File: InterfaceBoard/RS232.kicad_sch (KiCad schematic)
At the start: 0 parts

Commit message: InterfaceBoard: Add RS-232/DE-9
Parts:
- added C23, C24, C25, C26, C27: 1uF, Capacitor_SMD:C_0603_1608Metric, symbol Device:C_Small
- added J4: DB9_Female_MountingHoles, lib:ASSMANN_A-DF_09_A_KG-T2S, symbol Connector:DB9_Female_MountingHoles
- added R77: 0, Resistor_SMD:R_0603_1608Metric, symbol Device:R_Small
- added U3: MAX232, Package_SO:SOIC-16_3.9x9.9mm_P1.27mm, symbol Interface_UART:MAX232
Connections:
- new net: C24.1, U3.4 (C2+)
- new net: C24.2, U3.5 (C2-)
- new net: J4.0 (PAD), R77.1
- new net: C23.1, U3.1 (C1+)
- new net: C23.2, U3.3 (C1-)
- new net: J4.3, U3.13 (R1IN)
- new net: J4.2, U3.14 (T1OUT)
- new net: C25.1, U3.2 (VS+)
- new net: C26.1, U3.6 (VS-)
- new net: J4.8, U3.7 (T2OUT)
- new net: J4.7, U3.8 (R2IN)
- new net +5V: C27.1, U3.16 (VCC)
- new net GND: C25.2, C26.2, C27.2, J4.5, R77.2, U3.15 (GND)
- new net RS232_CTS: U3.10 (T2IN)
- new net RS232_RTS: U3.9 (R2OUT)
- new net RS232_RX: U3.12 (R1OUT)
- new net RS232_TX: U3.11 (T1IN)

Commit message: InterfaceBoard: Add 3.3 V regulater, test points.
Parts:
- U3: DigiKey (none) -> https://www.digikey.com/en/products/detail/texas-instrument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
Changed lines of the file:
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@@
+      (effects (font (size 1.27 1.27)) hide)
+    )
+    (property "DigiKey" "https://www.digikey.com/en/products/detail/texas-instruments/MAX232IDR/1511034" (id 4) (at 207.01 91.44 0)
       (effects (font (size 1.27 1.27)) hide)
     )

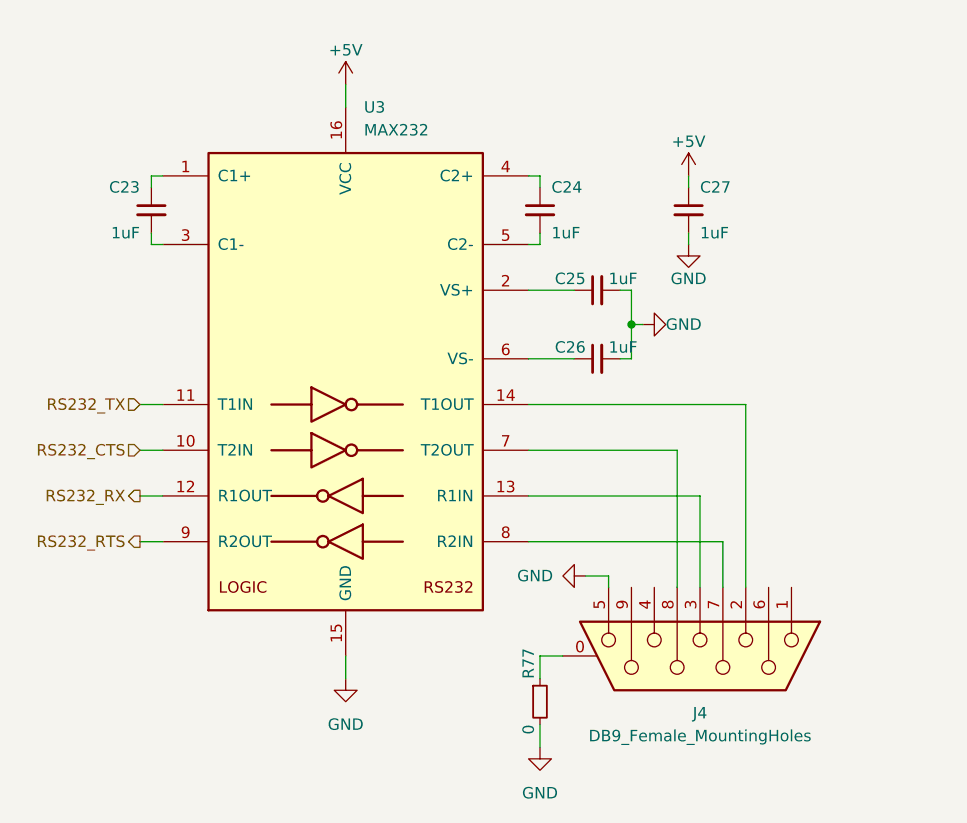
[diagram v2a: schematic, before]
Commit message: InterfaceBoard: MAX232 -> MAX3232
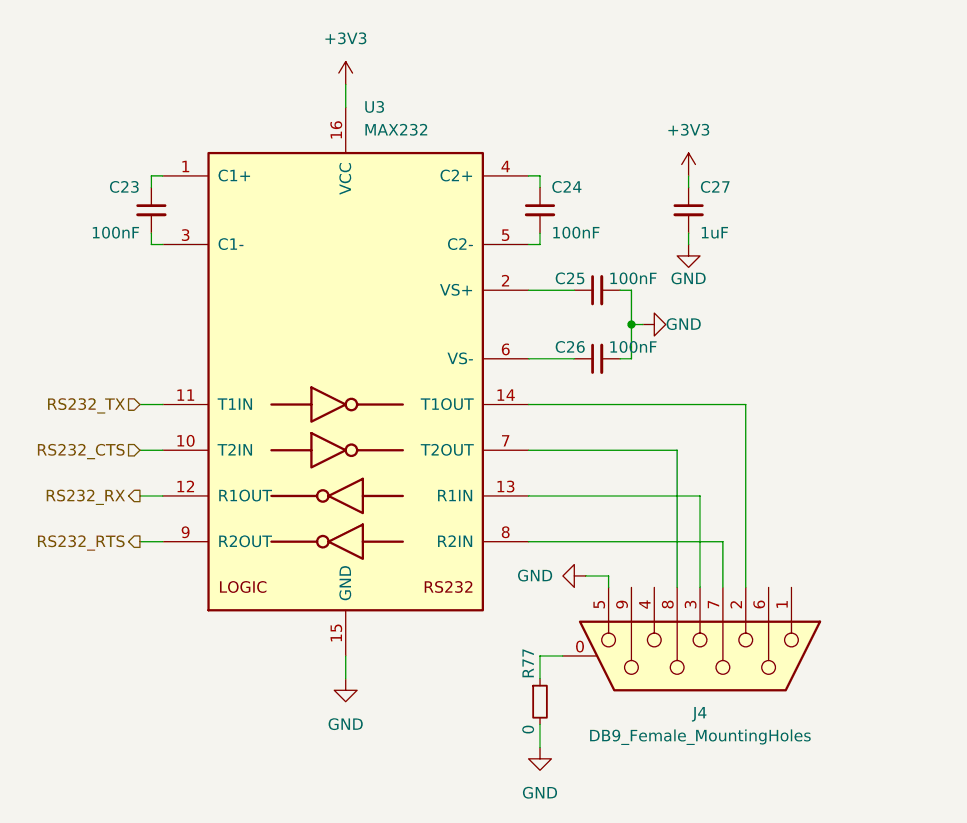
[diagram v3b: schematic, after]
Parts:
- C23, C24, C25, C26: value 1uF -> 100nF
- U3: symbol Interface_UART:MAX232 -> Interface_UART:MAX3232
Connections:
- net +5V renamed +3V3
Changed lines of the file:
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@@
     (effects (font (size 1.27 1.27)) (justify right))
   )
+  (symbol (lib_id "power:+3V3") (at 207.01 58.42 0) (unit 1)
+    (in_bom yes) (on_board yes) (fields_autoplaced)
+    (property "Reference" "#PWR?" (id 0) (at 207.01 62.23 0)
+      (effects (font (size 1.27 1.27)) hide)
+    )
+    (property "Value" "+3V3" (id 1) (at 207.01 53.34 0))
+    (property "Footprint" "" (id 2) (at 207.01 58.42 0)
+      (effects (font (size 1.27 1.27)) hide)
+    )
+    (property "Datasheet" "" (id 3) (at 207.01 58.42 0)
+      (effects (font (size 1.27 1.27)) hide)
+    )
+    (pin "1")
+  )
   (symbol (lib_id "Device:C_Small") (at 228.6 72.39 0) (mirror y) (unit 1)
     (in_bom yes) (on_board yes)
@@
       (effects (font (size 1.27 1.27)) (justify right))
     )
-    (property "Value" "1uF" (id 1) (at 229.87 74.93 0)
+    (property "Value" "100nF" (id 1) (at 229.87 74.93 0)
       (effects (font (size 1.27 1.27)) (justify right))
     )
@@
     (pin "2")
   )
-  (symbol (lib_id "power:+5V") (at 207.01 58.42 0) (unit 1)
-    (in_bom yes) (on_board yes)
-    (property "Reference" "#PWR0153" (id 0) (at 207.01 62.23 0)
-      (effects (font (size 1.27 1.27)) hide)
-    )
-    (property "Value" "+5V" (id 1) (at 207.01 54.61 0))
-    (property "Footprint" "" (id 2) (at 207.01 58.42 0)
-      (effects (font (size 1.27 1.27)) hide)
-    )
-    (property "Datasheet" "" (id 3) (at 207.01 58.42 0)
-      (effects (font (size 1.27 1.27)) hide)
-    )
-    (pin "1")
-  )
   (symbol (lib_id "Device:R_Small") (at 228.6 127 0) (unit 1)
     (in_bom yes) (on_board yes)
@@
       (effects (font (size 1.27 1.27)) (justify left))
     )
-    (property "Value" "1uF" (id 1) (at 184.15 74.93 0)
+    (property "Value" "100nF" (id 1) (at 184.15 74.93 0)
       (effects (font (size 1.27 1.27)) (justify left))
     )
@@
     (pin "2")
   )
-  (symbol (lib_id "Interface_UART:MAX232") (at 207.01 91.44 0) (unit 1)
+  (symbol (lib_id "Interface_UART:MAX3232") (at 207.01 91.44 0) (unit 1)
     (in_bom yes) (on_board yes) (fields_autoplaced)
     (property "Reference" "U3" (id 0) (at 209.0294 60.96 0)
@@
       (effects (font (size 1.27 1.27)) (justify left) hide)
     )
-    (property "Datasheet" "http://www.ti.com/lit/ds/symlink/max232.pdf" (id 3) (at 207.01 88.9 0)
+    (property "Datasheet" "https://datasheets.maximintegrated.com/en/ds/MAX3222-MAX3241.pdf" (id 3) (at 207.01 88.9 0)
       (effects (font (size 1.27 1.27)) hide)
     )
@@
       (effects (font (size 1.27 1.27)) (justify left))
     )
-    (property "Value" "1uF" (id 1) (at 236.22 87.63 90)
+    (property "Value" "100nF" (id 1) (at 236.22 87.63 90)
       (effects (font (size 1.27 1.27)) (justify right))
     )
@@
     (pin "1")
   )
-  (symbol (lib_id "power:+5V") (at 245.11 68.58 0) (unit 1)
-    (in_bom yes) (on_board yes)
-    (property "Reference" "#PWR0158" (id 0) (at 245.11 72.39 0)
-      (effects (font (size 1.27 1.27)) hide)
-    )
-    (property "Value" "+5V" (id 1) (at 245.11 64.77 0))
-    (property "Footprint" "" (id 2) (at 245.11 68.58 0)
-      (effects (font (size 1.27 1.27)) hide)
-    )
-    (property "Datasheet" "" (id 3) (at 245.11 68.58 0)
-      (effects (font (size 1.27 1.27)) hide)
-    )
-    (pin "1")
-  )
   (symbol (lib_id "power:GND") (at 207.01 124.46 0) (unit 1)
     (in_bom yes) (on_board yes) (fields_autoplaced)
@@
       (effects (font (size 1.27 1.27)) (justify left))
     )
-    (property "Value" "1uF" (id 1) (at 236.22 80.01 90)
+    (property "Value" "100nF" (id 1) (at 236.22 80.01 90)
       (effects (font (size 1.27 1.27)) (justify right))
     )
@@
       (effects (font (size 1.27 1.27)) hide)
     )
+    (pin "1")
+  )
+  (symbol (lib_id "power:+3V3") (at 245.11 68.58 0) (unit 1)
+    (in_bom yes) (on_board yes) (fields_autoplaced)
+    (property "Reference" "#PWR?" (id 0) (at 245.11 72.39 0)
+      (effects (font (size 1.27 1.27)) hide)
+    )
+    (property "Value" "+3V3" (id 1) (at 245.11 63.5 0))
+    (property "Footprint" "" (id 2) (at 245.11 68.58 0)
+      (effects (font (size 1.27 1.27)) hide)
+    )
+    (property "Datasheet" "" (id 3) (at 245.11 68.58 0)
+      (effects (font (size 1.27 1.27)) hide)
+    )

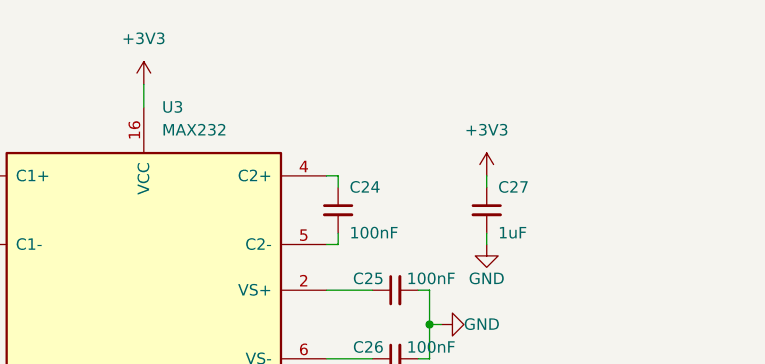
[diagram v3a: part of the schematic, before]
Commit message: InterfaceBoard: Routed Ethernet
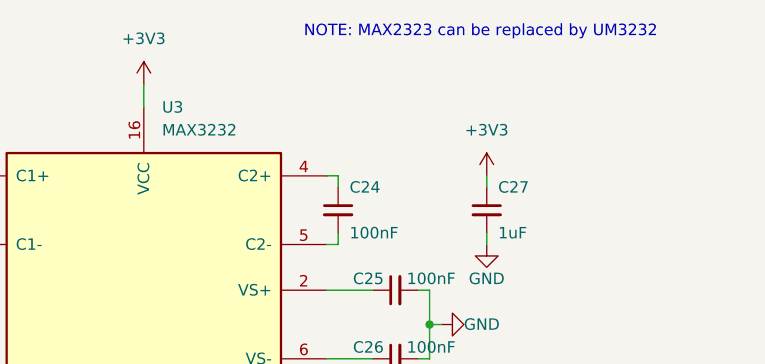
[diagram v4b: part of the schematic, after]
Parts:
- U3: value MAX232 -> MAX3232; DigiKey https://www.digikey.com/en/products/detail/texas-instruments/MAX232IDR/1511034 -> https://www.digikey.com/en/products/detail/texas-instruments/MAX3232EIDR/1089416?s=N4IgTCBcDaILYEMDGBmMaQF0C%2BQ
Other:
- note added: "NOTE: MAX2323 can be replaced by UM3232"
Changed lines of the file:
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@@
     (stroke (width 0) (type default) (color 0 0 0 0))
   )
+  (text "NOTE: MAX2323 can be replaced by UM3232" (at 224.79 53.34 0)
+    (effects (font (size 1.27 1.27)) (justify left bottom))
+  )
   (hierarchical_label "RS232_TX" (shape input) (at 184.15 93.98 180)
     (effects (font (size 1.27 1.27)) (justify right))
@@
   (symbol (lib_id "power:+3V3") (at 207.01 58.42 0) (unit 1)
     (in_bom yes) (on_board yes) (fields_autoplaced)
-    (property "Reference" "#PWR?" (id 0) (at 207.01 62.23 0)
+    (property "Reference" "#PWR0158" (id 0) (at 207.01 62.23 0)
       (effects (font (size 1.27 1.27)) hide)
     )
@@
       (effects (font (size 1.27 1.27)) (justify left))
     )
-    (property "Value" "MAX232" (id 1) (at 209.0294 63.5 0)
+    (property "Value" "MAX3232" (id 1) (at 209.0294 63.5 0)
       (effects (font (size 1.27 1.27)) (justify left))
     )
@@
       (effects (font (size 1.27 1.27)) (justify left) hide)
     )
-    (property "Datasheet" "https://datasheets.maximintegrated.com/en/ds/MAX3222-MAX3241.pdf" (id 3) (at 207.01 88.9 0)
-      (effects (font (size 1.27 1.27)) hide)
-    )
-    (property "DigiKey" "https://www.digikey.com/en/products/detail/texas-instruments/MAX232IDR/1511034" (id 4) (at 207.01 91.44 0)
+    (property "Datasheet" "https://www.ti.com/lit/ds/symlink/max3232e.pdf" (id 3) (at 207.01 88.9 0)
+      (effects (font (size 1.27 1.27)) hide)
+    )
+    (property "DigiKey" "https://www.digikey.com/en/products/detail/texas-instruments/MAX3232EIDR/1089416?s=N4IgTCBcDaILYEMDGBmMaQF0C%2BQ" (id 4) (at 207.01 91.44 0)
       (effects (font (size 1.27 1.27)) hide)
     )
@@
   (symbol (lib_id "power:+3V3") (at 245.11 68.58 0) (unit 1)
     (in_bom yes) (on_board yes) (fields_autoplaced)
-    (property "Reference" "#PWR?" (id 0) (at 245.11 72.39 0)
-      (effects (font (size 1.27 1.27)) hide)
-    )
+    (property "Reference" "#PWR0153" (id 0) (at 245.11 72.39 0)
+      (effects (font (size 1.27 1.27)) hide)
+    )

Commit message: InterfaceBoard: Rev 1.0
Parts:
- renumbered C27 to C17, C23 to C18, C24 to C19, C25 to C20, C26 to C21, J4 to J9, R77 to R90, U3 to U5
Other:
- company: (none) -> Peter Farley
- title: (none) -> Kiethley 615 Interface Board
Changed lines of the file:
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@@
 (kicad_sch (version 20211123) (generator eeschema)
   (paper "A4")
+  (title_block
+    (title "Kiethley 615 Interface Board")
+    (date "2023-03-04")
+    (rev "1.0")
+    (company "Peter Farley")
+    (comment 1 "Rev 1.0: Initial revision")
+  )
   (junction (at 238.76 85.09) (diameter 0) (color 0 0 0 0)
   )
@@
   (symbol (lib_id "Device:C_Small") (at 228.6 72.39 0) (mirror y) (unit 1)
     (in_bom yes) (on_board yes)
-    (property "Reference" "C24" (id 0) (at 229.87 69.85 0)
+    (property "Reference" "C19" (id 0) (at 229.87 69.85 0)
       (effects (font (size 1.27 1.27)) (justify right))
     )
@@
   (symbol (lib_id "Device:R_Small") (at 228.6 127 0) (unit 1)
     (in_bom yes) (on_board yes)
-    (property "Reference" "R77" (id 0) (at 227.33 124.46 90)
+    (property "Reference" "R90" (id 0) (at 227.33 124.46 90)
       (effects (font (size 1.27 1.27)) (justify left))
     )
@@
   (symbol (lib_id "Device:C_Small") (at 185.42 72.39 0) (mirror y) (unit 1)
     (in_bom yes) (on_board yes)
-    (property "Reference" "C23" (id 0) (at 184.15 69.85 0)
+    (property "Reference" "C18" (id 0) (at 184.15 69.85 0)
       (effects (font (size 1.27 1.27)) (justify left))
     )
@@
   (symbol (lib_id "Interface_UART:MAX3232") (at 207.01 91.44 0) (unit 1)
     (in_bom yes) (on_board yes) (fields_autoplaced)
-    (property "Reference" "U3" (id 0) (at 209.0294 60.96 0)
+    (property "Reference" "U5" (id 0) (at 209.0294 60.96 0)
       (effects (font (size 1.27 1.27)) (justify left))
     )
@@
   (symbol (lib_id "Device:C_Small") (at 245.11 72.39 0) (mirror y) (unit 1)
     (in_bom yes) (on_board yes)
-    (property "Reference" "C27" (id 0) (at 246.38 69.85 0)
+    (property "Reference" "C17" (id 0) (at 246.38 69.85 0)
       (effects (font (size 1.27 1.27)) (justify right))
     )
@@
   (symbol (lib_id "Device:C_Small") (at 234.95 88.9 90) (mirror x) (unit 1)
     (in_bom yes) (on_board yes)
-    (property "Reference" "C26" (id 0) (at 233.68 87.63 90)
+    (property "Reference" "C21" (id 0) (at 233.68 87.63 90)
       (effects (font (size 1.27 1.27)) (justify left))
     )
@@
   (symbol (lib_id "Connector:DB9_Female_MountingHoles") (at 246.38 121.92 270) (unit 1)
     (in_bom yes) (on_board yes) (fields_autoplaced)
-    (property "Reference" "J4" (id 0) (at 246.38 128.27 90))
+    (property "Reference" "J9" (id 0) (at 246.38 128.27 90))
     (property "Value" "DB9_Female_MountingHoles" (id 1) (at 246.38 130.81 90))
     (property "Footprint" "lib:ASSMANN_A-DF_09_A_KG-T2S" (id 2) (at 246.38 121.92 0)
@@
   (symbol (lib_id "Device:C_Small") (at 234.95 81.28 90) (mirror x) (unit 1)
     (in_bom yes) (on_board yes)
-    (property "Reference" "C25" (id 0) (at 233.68 80.01 90)
-      (effects (font (size 1.27 1.27)) (justify left))
-    )
+    (property "Reference" "C20" (id 0) (at 233.68 80.01 90)
+      (effects (font (size 1.27 1.27)) (justify left))
+    )

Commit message: InterfaceBoard: Add BOM
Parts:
- C17, C18, C19, C20, C21: DigiKey (none) -> https://www.digikey.com/en/products/detail/samsung-electro-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
- J9: DigiKey (none) -> https://www.digikey.com/en/products/detail/assmann-wsw-comp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
- R90: DigiKey (none) -> https://www.digikey.com/en/products/detail/walsin-technolog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
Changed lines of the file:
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@@
+      (effects (font (size 1.27 1.27)) hide)
+    )
+    (property "DigiKey" "https://www.digikey.com/en/products/detail/samsung-electro-mechanics/CL10B104KB8NNWC/3887593" (id 4) (at 228.6 72.39 0)
       (effects (font (size 1.27 1.27)) hide)
     )
@@
       (effects (font (size 1.27 1.27)) hide)
     )
+    (property "DigiKey" "https://www.digikey.com/en/products/detail/walsin-technology-corporation/WR06X000-PTL/5978108" (id 4) (at 228.6 127 0)
+      (effects (font (size 1.27 1.27)) hide)
+    )
     (pin "1")
     (pin "2")
@@
     )
     (property "Datasheet" "~" (id 3) (at 185.42 72.39 0)
+      (effects (font (size 1.27 1.27)) hide)
+    )
+    (property "DigiKey" "https://www.digikey.com/en/products/detail/samsung-electro-mechanics/CL10B104KB8NNWC/3887593" (id 4) (at 185.42 72.39 0)
       (effects (font (size 1.27 1.27)) hide)
     )
@@
       (effects (font (size 1.27 1.27)) hide)
     )
+    (property "DigiKey" "https://www.digikey.com/en/products/detail/samsung-electro-mechanics/CL10A105KA8NNNC/3886760" (id 4) (at 245.11 72.39 0)
+      (effects (font (size 1.27 1.27)) hide)
+    )
     (pin "1")
     (pin "2")
@@
     )
     (property "Datasheet" "~" (id 3) (at 234.95 88.9 0)
+      (effects (font (size 1.27 1.27)) hide)
+    )
+    (property "DigiKey" "https://www.digikey.com/en/products/detail/samsung-electro-mechanics/CL10B104KB8NNWC/3887593" (id 4) (at 234.95 88.9 0)
       (effects (font (size 1.27 1.27)) hide)
     )
@@
       (effects (font (size 1.27 1.27)) hide)
     )
-    (property "Datasheet" " ~" (id 3) (at 246.38 121.92 0)
+    (property "Datasheet" "http://www.assmann-wsw.com/uploads/datasheets/ASS_4888_CO.pdf" (id 3) (at 246.38 121.92 0)
+      (effects (font (size 1.27 1.27)) hide)
+    )
+    (property "DigiKey" "https://www.digikey.com/en/products/detail/assmann-wsw-components/A-DF-09-A-KG-T2S/1241800" (id 4) (at 246.38 121.92 0)
       (effects (font (size 1.27 1.27)) hide)
     )
@@
       (effects (font (size 1.27 1.27)) hide)
     )
+    (property "DigiKey" "https://www.digikey.com/en/products/detail/samsung-electro-mechanics/CL10B104KB8NNWC/3887593" (id 4) (at 234.95 81.28 0)
+      (effects (font (size 1.27 1.27)) hide)
+    )
